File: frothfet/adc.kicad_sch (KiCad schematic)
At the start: 15 parts, among them U18 MCP3564R

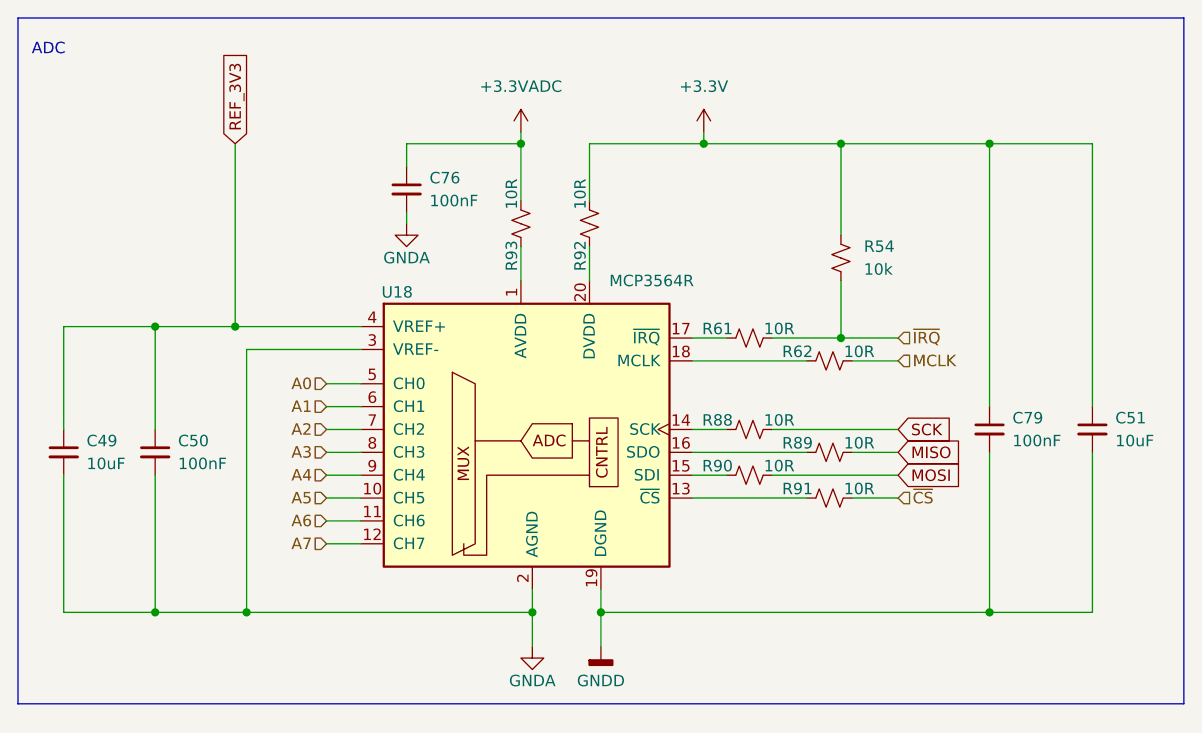
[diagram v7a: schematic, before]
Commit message: consolidated on a single adc
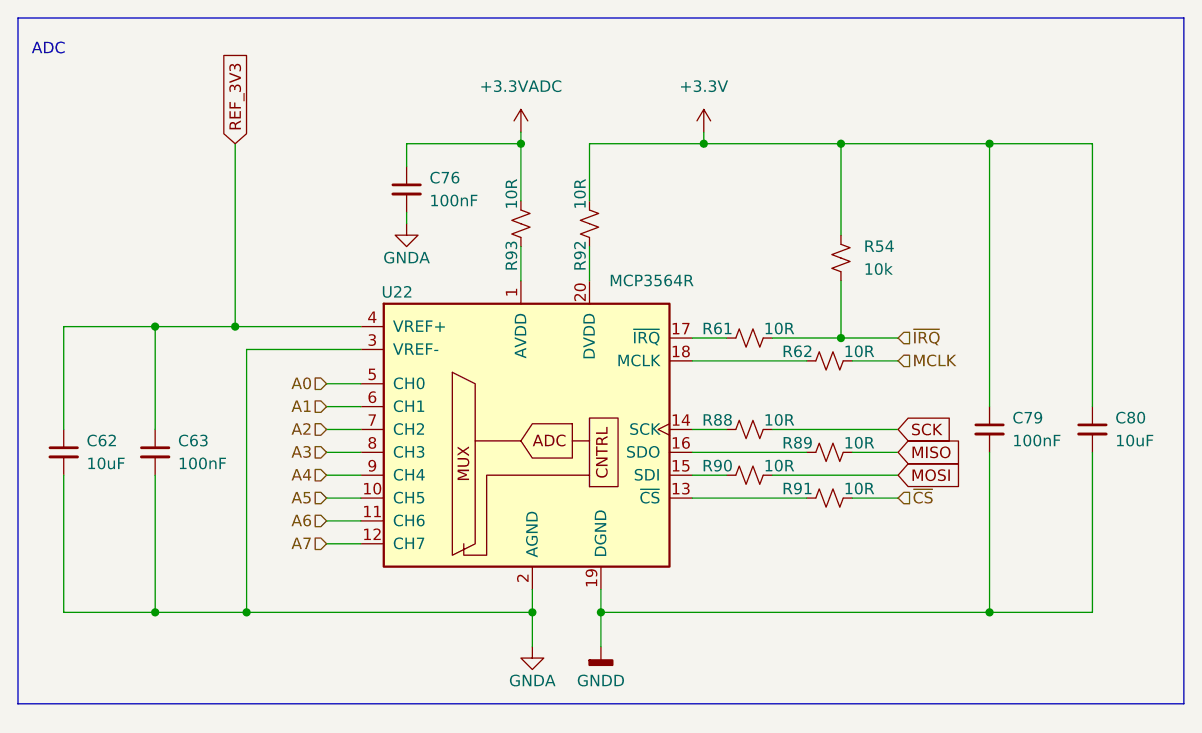
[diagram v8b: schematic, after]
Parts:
- renumbered C49 to C62, C50 to C63, C51 to C80, U18 to U22
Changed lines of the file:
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@@
 		(on_board yes)
 		(dnp no)
-		(property "Reference" "C50"
+		(property "Reference" "C63"
 			(at 97.79 87.6363 0)
 			(effects
@@
 		)
 		(instances
-			(project ""
-				(path "/c83c6236-96e9-46ad-9d7a-9e2efa4a7966/b87f80e1-ecbd-4ee0-be26-4b252158928b"
-					(reference "C50")
+			(project "frothfet"
+				(path "/c83c6236-96e9-46ad-9d7a-9e2efa4a7966/6b72210f-69d1-4134-acd2-eb4247fc5d85"
+					(reference "C63")
 					(unit 1)
 				)
@@
 		(dnp no)
 		(fields_autoplaced yes)
-		(property "Reference" "#PWR064"
+		(property "Reference" "#PWR079"
 			(at 156.21 57.15 0)
 			(effects
@@
 		)
 		(instances
-			(project ""
-				(path "/c83c6236-96e9-46ad-9d7a-9e2efa4a7966/b87f80e1-ecbd-4ee0-be26-4b252158928b"
-					(reference "#PWR064")
+			(project "frothfet"
+				(path "/c83c6236-96e9-46ad-9d7a-9e2efa4a7966/6b72210f-69d1-4134-acd2-eb4247fc5d85"
+					(reference "#PWR079")
 					(unit 1)
 				)
@@
 		(on_board yes)
 		(dnp no)
-		(property "Reference" "#PWR062"
+		(property "Reference" "#PWR077"
 			(at 137.16 116.84 0)
 			(effects
@@
 		)
 		(instances
-			(project ""
-				(path "/c83c6236-96e9-46ad-9d7a-9e2efa4a7966/b87f80e1-ecbd-4ee0-be26-4b252158928b"
-					(reference "#PWR062")
+			(project "frothfet"
+				(path "/c83c6236-96e9-46ad-9d7a-9e2efa4a7966/6b72210f-69d1-4134-acd2-eb4247fc5d85"
+					(reference "#PWR077")
 					(unit 1)
 				)
@@
 		(dnp no)
 		(fields_autoplaced yes)
-		(property "Reference" "#PWR063"
+		(property "Reference" "#PWR078"
 			(at 144.78 116.84 0)
 			(effects
@@
 		)
 		(instances
-			(project ""
-				(path "/c83c6236-96e9-46ad-9d7a-9e2efa4a7966/b87f80e1-ecbd-4ee0-be26-4b252158928b"
-					(reference "#PWR063")
+			(project "frothfet"
+				(path "/c83c6236-96e9-46ad-9d7a-9e2efa4a7966/6b72210f-69d1-4134-acd2-eb4247fc5d85"
+					(reference "#PWR078")
 					(unit 1)
 				)
@@
 		(on_board yes)
 		(dnp no)
-		(property "Reference" "C49"
+		(property "Reference" "C62"
 			(at 87.63 87.6363 0)
 			(effects
@@
 		)
 		(instances
-			(project "frothfet-12ch"
-				(path "/c83c6236-96e9-46ad-9d7a-9e2efa4a7966/b87f80e1-ecbd-4ee0-be26-4b252158928b"
-					(reference "C49")
+			(project "frothfet"
+				(path "/c83c6236-96e9-46ad-9d7a-9e2efa4a7966/6b72210f-69d1-4134-acd2-eb4247fc5d85"
+					(reference "C62")
 					(unit 1)
 				)
@@
 		(on_board yes)
 		(dnp no)
-		(property "Reference" "C51"
+		(property "Reference" "C80"
 			(at 201.93 85.0963 0)
 			(effects
@@
 		)
 		(instances
-			(project ""
-				(path "/c83c6236-96e9-46ad-9d7a-9e2efa4a7966/b87f80e1-ecbd-4ee0-be26-4b252158928b"
-					(reference "C51")
+			(project "frothfet"
+				(path "/c83c6236-96e9-46ad-9d7a-9e2efa4a7966/6b72210f-69d1-4134-acd2-eb4247fc5d85"
+					(reference "C80")
 					(unit 1)
 				)
@@
 		(instances
 			(project "frothfet"
+				(path "/c83c6236-96e9-46ad-9d7a-9e2efa4a7966/6b72210f-69d1-4134-acd2-eb4247fc5d85"
+					(reference "R39")
+					(unit 1)
+				)
 				(path "/c83c6236-96e9-46ad-9d7a-9e2efa4a7966/b87f80e1-ecbd-4ee0-be26-4b252158928b"
 					(reference "R89")
@@
 		(instances
 			(project "frothfet"
+				(path "/c83c6236-96e9-46ad-9d7a-9e2efa4a7966/6b72210f-69d1-4134-acd2-eb4247fc5d85"
+					(reference "R21")
+					(unit 1)
+				)
 				(path "/c83c6236-96e9-46ad-9d7a-9e2efa4a7966/b87f80e1-ecbd-4ee0-be26-4b252158928b"
 					(reference "R88")
@@
 		(instances
 			(project "frothfet"
+				(path "/c83c6236-96e9-46ad-9d7a-9e2efa4a7966/6b72210f-69d1-4134-acd2-eb4247fc5d85"
+					(reference "R3")
+					(unit 1)
+				)
 				(path "/c83c6236-96e9-46ad-9d7a-9e2efa4a7966/b87f80e1-ecbd-4ee0-be26-4b252158928b"
 					(reference "R93")
@@
 		(instances
 			(project "frothfet"
+				(path "/c83c6236-96e9-46ad-9d7a-9e2efa4a7966/6b72210f-69d1-4134-acd2-eb4247fc5d85"
+					(reference "R27")
+					(unit 1)
+				)
 				(path "/c83c6236-96e9-46ad-9d7a-9e2efa4a7966/b87f80e1-ecbd-4ee0-be26-4b252158928b"
 					(reference "R90")
@@
 		(instances
 			(project "frothfet"
+				(path "/c83c6236-96e9-46ad-9d7a-9e2efa4a7966/6b72210f-69d1-4134-acd2-eb4247fc5d85"
+					(reference "R15")
+					(unit 1)
+				)
 				(path "/c83c6236-96e9-46ad-9d7a-9e2efa4a7966/b87f80e1-ecbd-4ee0-be26-4b252158928b"
 					(reference "R61")
@@
 		(instances
 			(project "frothfet"
+				(path "/c83c6236-96e9-46ad-9d7a-9e2efa4a7966/6b72210f-69d1-4134-acd2-eb4247fc5d85"
+					(reference "#PWR06")
+					(unit 1)
+				)
 				(path "/c83c6236-96e9-46ad-9d7a-9e2efa4a7966/b87f80e1-ecbd-4ee0-be26-4b252158928b"
 					(reference "#PWR083")
@@
 		(instances
 			(project "frothfet"
+				(path "/c83c6236-96e9-46ad-9d7a-9e2efa4a7966/6b72210f-69d1-4134-acd2-eb4247fc5d85"
+					(reference "R9")
+					(unit 1)
+				)
 				(path "/c83c6236-96e9-46ad-9d7a-9e2efa4a7966/b87f80e1-ecbd-4ee0-be26-4b252158928b"
 					(reference "R92")
@@
 		(instances
 			(project "frothfet"
+				(path "/c83c6236-96e9-46ad-9d7a-9e2efa4a7966/6b72210f-69d1-4134-acd2-eb4247fc5d85"
+					(reference "R33")
+					(unit 1)
+				)
 				(path "/c83c6236-96e9-46ad-9d7a-9e2efa4a7966/b87f80e1-ecbd-4ee0-be26-4b252158928b"
 					(reference "R62")
@@
 		(instances
 			(project "frothfet"
+				(path "/c83c6236-96e9-46ad-9d7a-9e2efa4a7966/6b72210f-69d1-4134-acd2-eb4247fc5d85"
+					(reference "C64")
+					(unit 1)
+				)
 				(path "/c83c6236-96e9-46ad-9d7a-9e2efa4a7966/b87f80e1-ecbd-4ee0-be26-4b252158928b"
 					(reference "C76")
@@
 		(instances
 			(project "frothfet"
+				(path "/c83c6236-96e9-46ad-9d7a-9e2efa4a7966/6b72210f-69d1-4134-acd2-eb4247fc5d85"
+					(reference "R45")
+					(unit 1)
+				)
 				(path "/c83c6236-96e9-46ad-9d7a-9e2efa4a7966/b87f80e1-ecbd-4ee0-be26-4b252158928b"
 					(reference "R91")
@@
 		(instances
 			(project "frothfet"
+				(path "/c83c6236-96e9-46ad-9d7a-9e2efa4a7966/6b72210f-69d1-4134-acd2-eb4247fc5d85"
+					(reference "#PWR03")
+					(unit 1)
+				)
 				(path "/c83c6236-96e9-46ad-9d7a-9e2efa4a7966/b87f80e1-ecbd-4ee0-be26-4b252158928b"
 					(reference "#PWR084")
@@
 		(instances
 			(project "frothfet"
+				(path "/c83c6236-96e9-46ad-9d7a-9e2efa4a7966/6b72210f-69d1-4134-acd2-eb4247fc5d85"
+					(reference "C65")
+					(unit 1)
+				)
 				(path "/c83c6236-96e9-46ad-9d7a-9e2efa4a7966/b87f80e1-ecbd-4ee0-be26-4b252158928b"
 					(reference "C79")
@@
 		(on_board yes)
 		(dnp no)
-		(property "Reference" "U18"
+		(property "Reference" "U22"
 			(at 120.396 71.12 0)
 			(effects
@@
 		)
 		(instances
-			(project ""
-				(path "/c83c6236-96e9-46ad-9d7a-9e2efa4a7966/b87f80e1-ecbd-4ee0-be26-4b252158928b"
-					(reference "U18")
+			(project "frothfet"
+				(path "/c83c6236-96e9-46ad-9d7a-9e2efa4a7966/6b72210f-69d1-4134-acd2-eb4247fc5d85"
+					(reference "U22")
 					(unit 1)
 				)
@@
 		(instances
 			(project "frothfet"
+				(path "/c83c6236-96e9-46ad-9d7a-9e2efa4a7966/6b72210f-69d1-4134-acd2-eb4247fc5d85"
+					(reference "R71")
+					(unit 1)
+				)
 				(path "/c83c6236-96e9-46ad-9d7a-9e2efa4a7966/b87f80e1-ecbd-4ee0-be26-4b252158928b"
 					(reference "R54")
